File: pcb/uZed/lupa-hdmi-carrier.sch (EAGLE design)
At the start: 95 parts, among them K1 694108105102

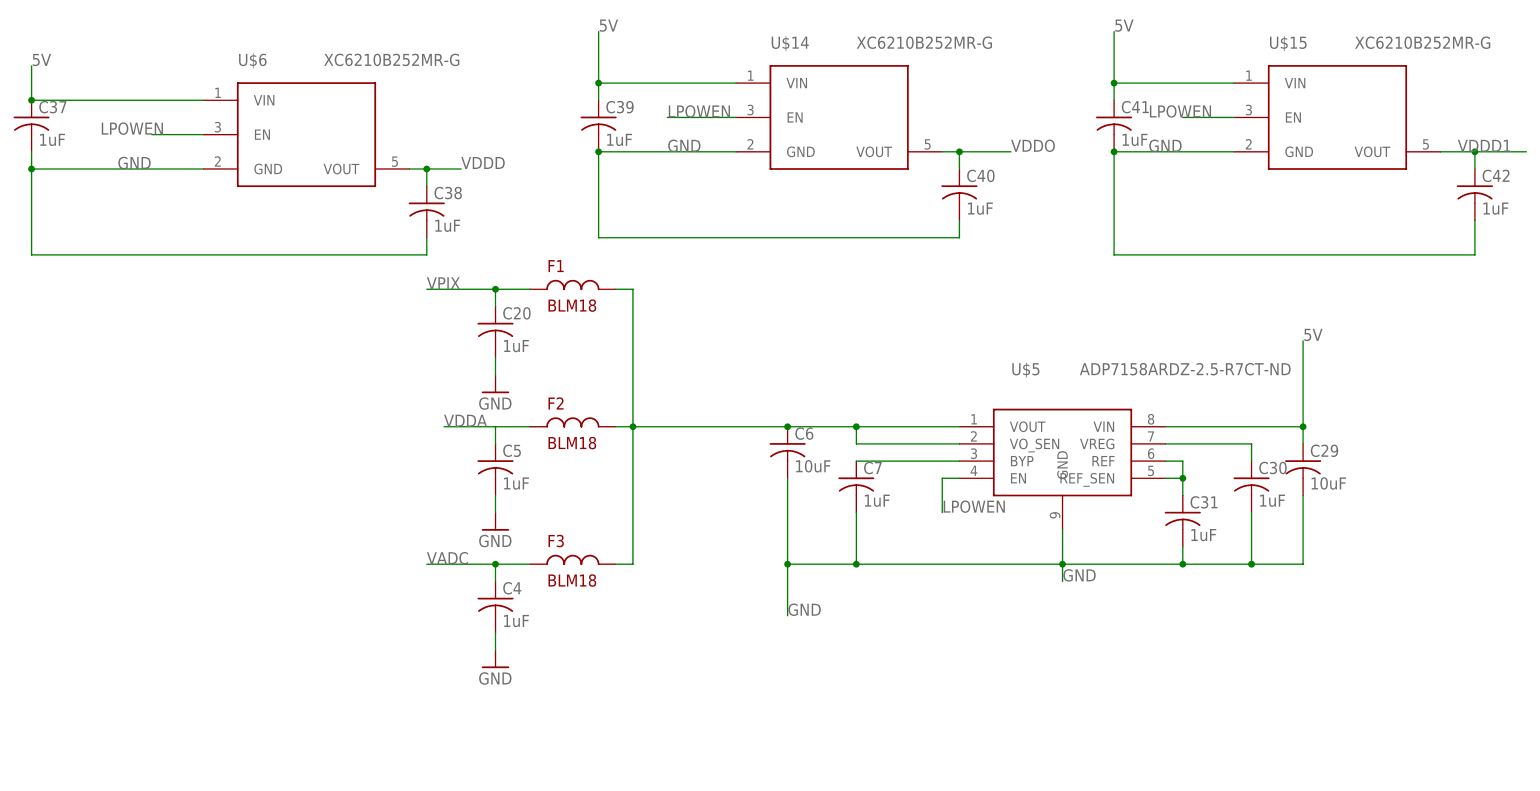
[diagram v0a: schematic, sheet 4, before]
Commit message: added images and silkscreen tweaks on pcb layout. fixed cap lableling.
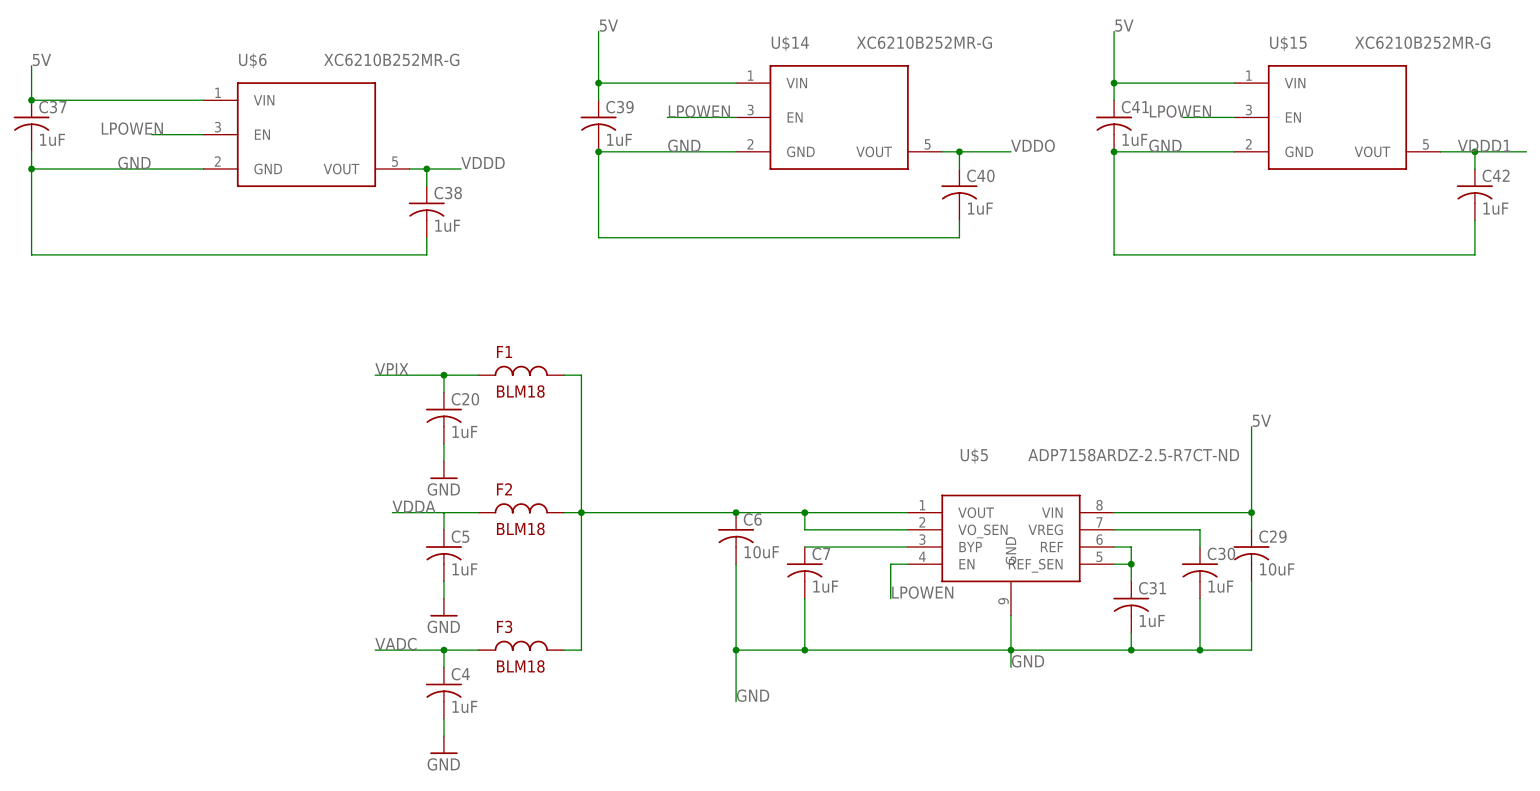
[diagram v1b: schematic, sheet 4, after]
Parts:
- C22, C23, C26, C27: value (none) -> .1uF
- C24, C25: value .1uf -> .1uF
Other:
- moved on the sheet: C11, C16, C17, C18, C19, C20, C29, C30, C31, C4, C5, C6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
